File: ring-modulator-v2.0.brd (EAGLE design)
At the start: 34.3 x 24.1 mm, 26 parts, among them IC1 TL072D, U1 MC1496DR2G

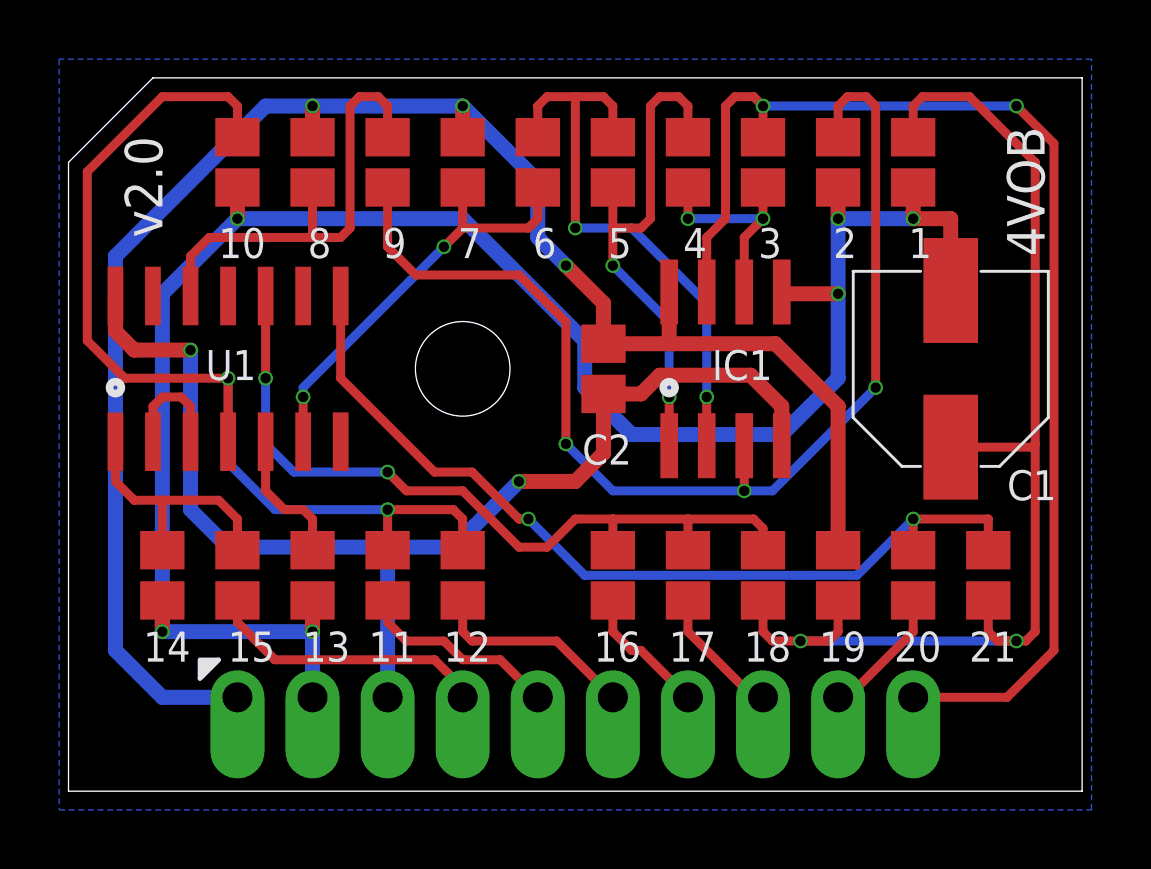
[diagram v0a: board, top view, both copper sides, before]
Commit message: Added smd assembly bom etc
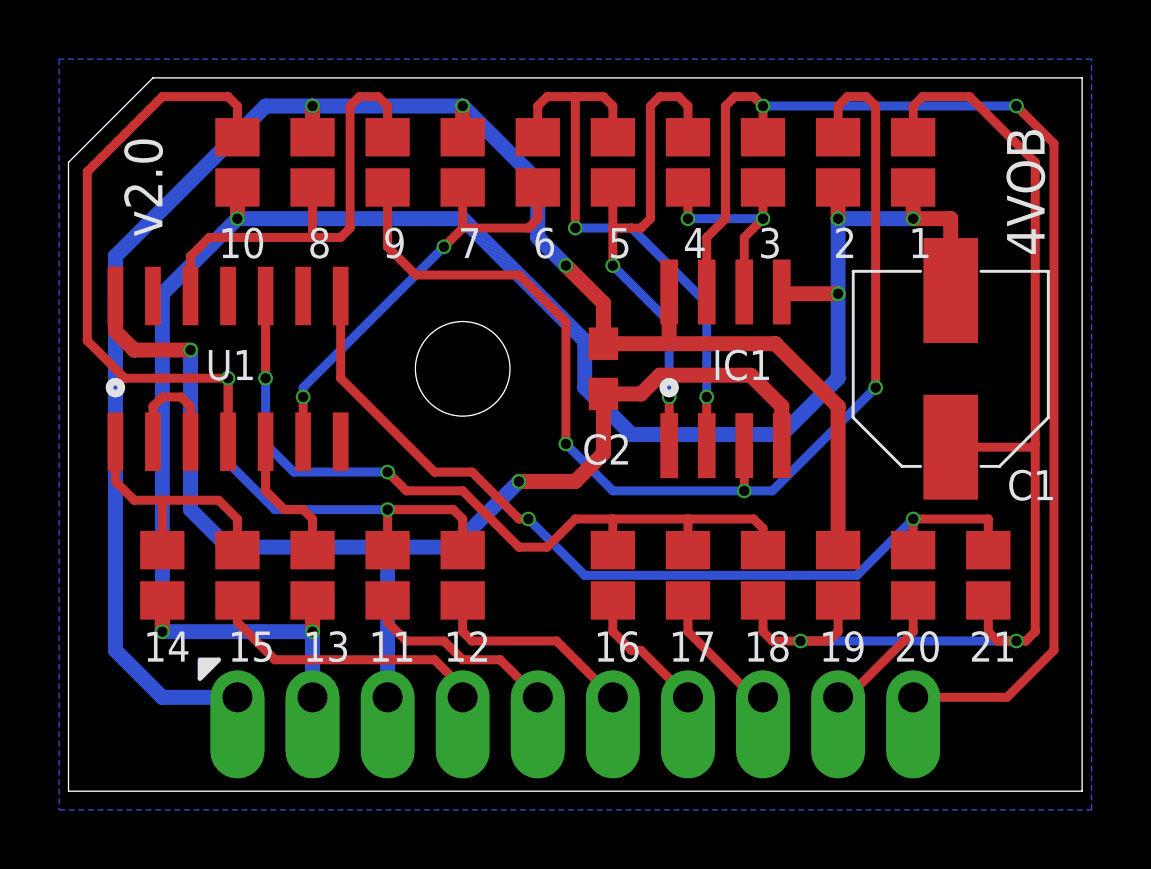
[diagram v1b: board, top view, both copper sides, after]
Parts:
- C1: value 100u 16V -> 100u 25V
- C2: device resistor:C0805 -> rcl:C0603
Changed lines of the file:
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@@
 <attribute name="VALUE" x="28.321" y="6.5405" size="1.27" layer="27" rot="R90"/>
 </element>
-<element name="C1" library="joakim-jclpcb" package="CAPAE660X610N" value="100u 16V" x="29.845" y="14.2875" smashed="yes" rot="R90">
+<element name="C1" library="joakim-jclpcb" package="CAPAE660X610N" value="100u 25V" x="29.845" y="14.2875" smashed="yes" rot="R90">
 <attribute name="DESCRIPTION" value="Aluminum Electrolytic Capacitors - SMD 100uF 16 Volts 20%" x="29.845" y="14.2875" size="1.778" layer="27" rot="R90" display="off"/>
 <attribute name="HEIGHT" value="6.1mm" x="29.845" y="14.2875" size="1.778" layer="27" rot="R90" display="off"/>
@@
 <attribute name="VALUE" x="26.162" y="12.3825" size="1.27" layer="27" rot="R90"/>
 </element>
-<element name="C2" library="resistor" package="C0805" value="100n" x="18.0975" y="14.2875" smashed="yes" rot="R90">
+<element name="C2" library="rcl" library_urn="urn:adsk.eagle:library:334" package="C0603" package3d_urn="urn:adsk.eagle:package:23616/2" value="100n" x="18.0975" y="14.2875" smashed="yes" rot="R90">
+<attribute name="POPULARITY" value="73" x="18.0975" y="14.2875" size="1.778" layer="27" rot="R90" display="off"/>
+<attribute name="SPICEPREFIX" value="C" x="18.0975" y="14.2875" size="1.778" layer="27" rot="R90" display="off"/>
 <attribute name="VALUE" x="20.3835" y="13.3985" size="1.27" layer="27" rot="R90"/>
 </element>
@@
 </board>
 </drawing>
+<compatibility>
+<note version="8.2" severity="warning">
+Since Version 8.2, EAGLE supports online libraries. The ids
+of those online libraries will not be understood (or retained)
+with this version.
+</note>
+<note version="8.3" severity="warning">
+Since Version 8.3, EAGLE supports URNs for individual library
+assets (packages, symbols, and devices). The URNs of those assets
+will not be understood (or retained) with this version.
+</note>
+<note version="8.3" severity="warning">
+Since Version 8.3, EAGLE supports the association of 3D packages
+with devices in libraries, schematics, and board files. Those 3D
+packages will not be understood (or retained) with this version.
+</note>
+</compatibility>
 </eagle>

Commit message: Added info about external trimmers
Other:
- board text added: "AGND"
- board text removed: "Gnd"
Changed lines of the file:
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@@
 <grid distance="12.5" unitdist="mil" unit="mil" style="dots" multiple="1" display="yes" altdistance="0.025" altunitdist="inch" altunit="inch"/>
 <layers>
-<layer number="1" name="Top" color="4" fill="1" visible="yes" active="yes"/>
+<layer number="1" name="Top" color="4" fill="1" visible="no" active="yes"/>
 <layer number="2" name="Route2" color="1" fill="3" visible="no" active="no"/>
 <layer number="3" name="Route3" color="4" fill="3" visible="no" active="no"/>
@@
 <layer number="19" name="Unrouted" color="6" fill="1" visible="yes" active="yes"/>
 <layer number="20" name="Dimension" color="15" fill="1" visible="yes" active="yes"/>
-<layer number="21" name="tPlace" color="7" fill="1" visible="yes" active="yes"/>
+<layer number="21" name="tPlace" color="7" fill="1" visible="no" active="yes"/>
 <layer number="22" name="bPlace" color="7" fill="1" visible="yes" active="yes"/>
-<layer number="23" name="tOrigins" color="15" fill="1" visible="yes" active="yes"/>
+<layer number="23" name="tOrigins" color="15" fill="1" visible="no" active="yes"/>
 <layer number="24" name="bOrigins" color="15" fill="1" visible="yes" active="yes"/>
-<layer number="25" name="tNames" color="7" fill="1" visible="yes" active="yes"/>
+<layer number="25" name="tNames" color="7" fill="1" visible="no" active="yes"/>
 <layer number="26" name="bNames" color="7" fill="1" visible="yes" active="yes"/>
 <layer number="27" name="tValues" color="7" fill="1" visible="no" active="yes"/>
@@
 <layer number="37" name="tTest" color="7" fill="1" visible="no" active="yes"/>
 <layer number="38" name="bTest" color="7" fill="1" visible="no" active="yes"/>
-<layer number="39" name="tKeepout" color="4" fill="11" visible="yes" active="yes"/>
+<layer number="39" name="tKeepout" color="4" fill="11" visible="no" active="yes"/>
 <layer number="40" name="bKeepout" color="1" fill="11" visible="yes" active="yes"/>
-<layer number="41" name="tRestrict" color="4" fill="10" visible="yes" active="yes"/>
+<layer number="41" name="tRestrict" color="4" fill="10" visible="no" active="yes"/>
 <layer number="42" name="bRestrict" color="1" fill="10" visible="yes" active="yes"/>
 <layer number="43" name="vRestrict" color="2" fill="10" visible="no" active="yes"/>
@@
 <layer number="49" name="Reference" color="7" fill="1" visible="no" active="yes"/>
 <layer number="50" name="dxf" color="7" fill="1" visible="no" active="no"/>
-<layer number="51" name="tDocu" color="7" fill="1" visible="yes" active="yes"/>
+<layer number="51" name="tDocu" color="7" fill="1" visible="no" active="yes"/>
 <layer number="52" name="bDocu" color="7" fill="1" visible="yes" active="yes"/>
 <layer number="53" name="tGND_GNDA" color="7" fill="9" visible="no" active="no"/>
@@
 <text x="5.08" y="4.445" size="1.27" layer="26" font="vector" rot="MR90">+15v</text>
 <text x="10.16" y="4.445" size="1.27" layer="26" font="vector" rot="MR90">-15v</text>
-<text x="7.62" y="4.445" size="1.27" layer="26" font="vector" rot="MR90">Gnd</text>
+<text x="7.62" y="4.445" size="1.27" layer="26" font="vector" rot="MR90">AGND</text>
 <text x="17.78" y="4.445" size="1.27" layer="26" font="vector" rot="MR90">Signal</text>
 <text x="20.32" y="4.445" size="1.27" layer="26" font="vector" rot="MR90">Carrier</text>
